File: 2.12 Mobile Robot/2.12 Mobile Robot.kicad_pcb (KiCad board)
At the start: 2 copper layers, 63 parts, among them J1 Motor Control L, J2 Motor Control R, J3 GND, J4 3.3V, J5 UART, J6 5V, J8 Power IO, Q1 DMMT5401-7-F, Q2 DMG2305UX-13, SW1 RST_SW, SW2 BOOT_SW, SW3 SW_PWR, SW4 SW_PWR, U1 ProS3, U2 TCA9548APWR, U3 MOTOR_PWR, U4 POWER_IN, U5 TPS564208DDCT

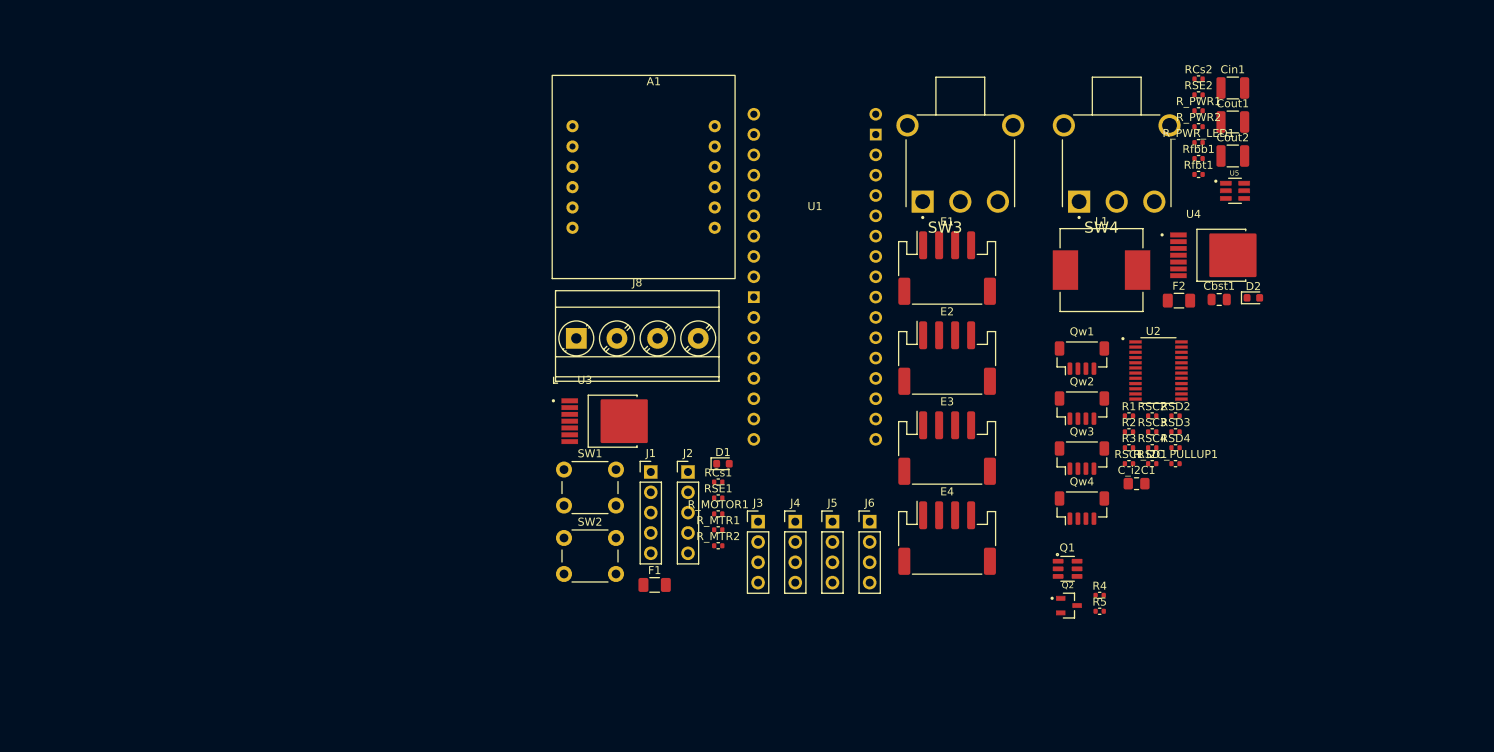
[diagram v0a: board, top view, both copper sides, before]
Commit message: Renamed stuff
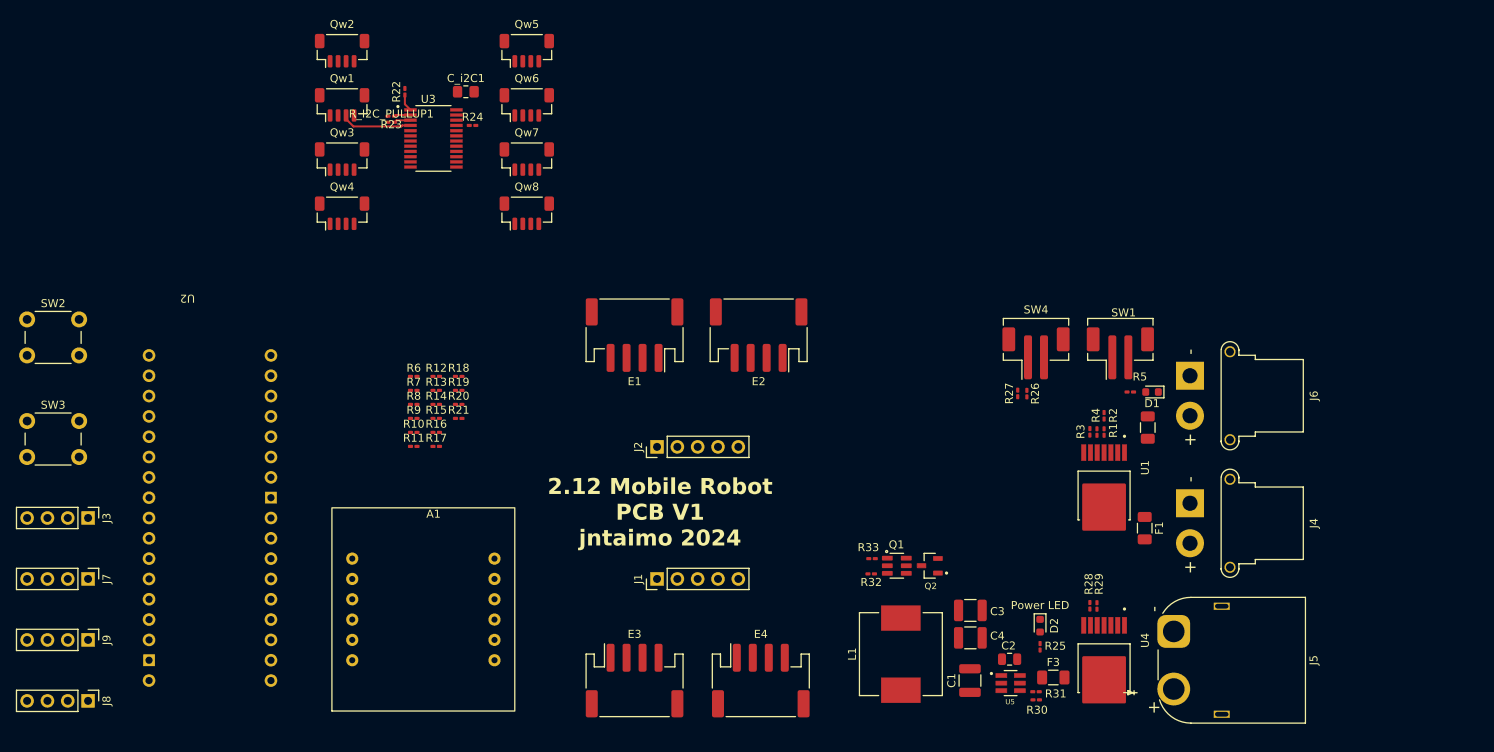
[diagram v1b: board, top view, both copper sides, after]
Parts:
- removed Cbst1: 0.1uF, Capacitor_SMD:C_0805_2012Metric
- removed Cin1: 10uF, Capacitor_SMD:C_1210_3225Metric
- removed Cout1, Cout2: 22uF, Capacitor_SMD:C_1210_3225Metric
- removed the F2 at (170.7, 89.7)
- removed the J8 at (95.3, 94.4)
- removed RCs2, RSE2, R_PWR1, R_PWR2: 15k, Resistor_SMD:R_0402_1005Metric
- removed RSC1, RSC2, RSC3, RSC4, RSD1, RSD2, RSD3, RSD4, Rfbb1: 10k, Resistor_SMD:R_0402_1005Metric
- removed R_PWR_LED1: 1kΩ, Resistor_SMD:R_0402_1005Metric
- removed Rfbt1: 56.2k, Resistor_SMD:R_0402_1005Metric
- added C1: 10uF, Capacitor_SMD:C_1210_3225Metric, F.Cu at (144.5, 137.2)
- added C2: 0.1uF, Capacitor_SMD:C_0805_2012Metric, F.Cu at (149.5, 134.5)
- added C3: 22uF, Capacitor_SMD:C_1210_3225Metric, F.Cu at (144.6, 128.4)
- added C4: 22uF, Capacitor_SMD:C_1210_3225Metric, F.Cu at (144.6, 131.8)
- added F1: 20A, Fuse:Fuse_1206_3216Metric, F.Cu at (166.4, 118.1)
- added F3: 20A, Fuse:Fuse_1206_3216Metric, F.Cu at (154.9, 136.8)
- added J4: Motor Power R, Connector_AMASS:AMASS_XT30PW-F_1x02_P2.50mm_Horizontal, F.Cu at (172.0, 115.0)
- added J5: Battery Power, Connector_AMASS:AMASS_XT60PW-M_1x02_P7.20mm_Horizontal, F.Cu at (170.0, 131.0)
- added J6: Motor Power L, Connector_AMASS:AMASS_XT30PW-F_1x02_P2.50mm_Horizontal, F.Cu at (172.0, 99.1)
- added Qw5: Qwiic, Connector_JST:JST_SH_BM04B-SRSS-TB_1x04-1MP_P1.00mm_Vertical, F.Cu at (89.1, 58.4)
- added Qw6: Qwiic, Connector_JST:JST_SH_BM04B-SRSS-TB_1x04-1MP_P1.00mm_Vertical, F.Cu at (89.1, 65.2)
- added Qw7: Qwiic, Connector_JST:JST_SH_BM04B-SRSS-TB_1x04-1MP_P1.00mm_Vertical, F.Cu at (89.1, 72.0)
- added Qw8: Qwiic, Connector_JST:JST_SH_BM04B-SRSS-TB_1x04-1MP_P1.00mm_Vertical, F.Cu at (89.1, 78.7)
- added R10: 10K, Resistor_SMD:R_0201_0603Metric_Pad0.64x0.40mm_HandSolder, F.Cu at (75.0, 106.1)
- added R11: 10K, Resistor_SMD:R_0201_0603Metric_Pad0.64x0.40mm_HandSolder, F.Cu at (75.0, 107.9)
- added R12: 10K, Resistor_SMD:R_0201_0603Metric_Pad0.64x0.40mm_HandSolder, F.Cu at (77.8, 99.1)
- added R13: 10K, Resistor_SMD:R_0201_0603Metric_Pad0.64x0.40mm_HandSolder, F.Cu at (77.8, 100.9)
- added R14: 10K, Resistor_SMD:R_0201_0603Metric_Pad0.64x0.40mm_HandSolder, F.Cu at (77.8, 102.6)
- added R15: 10K, Resistor_SMD:R_0201_0603Metric_Pad0.64x0.40mm_HandSolder, F.Cu at (77.8, 104.4)
- added R16: 10K, Resistor_SMD:R_0201_0603Metric_Pad0.64x0.40mm_HandSolder, F.Cu at (77.8, 106.1)
- added R17: 10K, Resistor_SMD:R_0201_0603Metric_Pad0.64x0.40mm_HandSolder, F.Cu at (77.8, 107.9)
- added R18: 10K, Resistor_SMD:R_0201_0603Metric_Pad0.64x0.40mm_HandSolder, F.Cu at (80.6, 99.1)
- added R19: 10K, Resistor_SMD:R_0201_0603Metric_Pad0.64x0.40mm_HandSolder, F.Cu at (80.6, 100.9)
- added R20: 10K, Resistor_SMD:R_0201_0603Metric_Pad0.64x0.40mm_HandSolder, F.Cu at (80.6, 102.6)
- added R21: 10K, Resistor_SMD:R_0201_0603Metric_Pad0.64x0.40mm_HandSolder, F.Cu at (80.6, 104.4)
- added R25: 1kΩ, Resistor_SMD:R_0201_0603Metric_Pad0.64x0.40mm_HandSolder, F.Cu at (153.3, 132.9)
- added R26: 15k, Resistor_SMD:R_0201_0603Metric_Pad0.64x0.40mm_HandSolder, F.Cu at (151.6, 101.3)
- added R27: 15k, Resistor_SMD:R_0201_0603Metric_Pad0.64x0.40mm_HandSolder, F.Cu at (150.5, 101.3)
- added R28: 15k, Resistor_SMD:R_0201_0603Metric_Pad0.64x0.40mm_HandSolder, F.Cu at (159.5, 127.8)
- added R29: 15k, Resistor_SMD:R_0201_0603Metric_Pad0.64x0.40mm_HandSolder, F.Cu at (160.4, 127.8)
- added R30: 56.2k, Resistor_SMD:R_0201_0603Metric_Pad0.64x0.40mm_HandSolder, F.Cu at (152.8, 139.6)
- added R31: 10k, Resistor_SMD:R_0201_0603Metric_Pad0.64x0.40mm_HandSolder, F.Cu at (152.8, 138.6)
- added R6: 10K, Resistor_SMD:R_0201_0603Metric_Pad0.64x0.40mm_HandSolder, F.Cu at (75.0, 99.1)
- added R7: 10K, Resistor_SMD:R_0201_0603Metric_Pad0.64x0.40mm_HandSolder, F.Cu at (75.0, 100.9)
- added R8: 10K, Resistor_SMD:R_0201_0603Metric_Pad0.64x0.40mm_HandSolder, F.Cu at (75.0, 102.6)
- added R9: 10K, Resistor_SMD:R_0201_0603Metric_Pad0.64x0.40mm_HandSolder, F.Cu at (75.0, 104.4)
- R1: renamed from R_MTR1; footprint Resistor_SMD:R_0402_1005Metric -> Resistor_SMD:R_0201_0603Metric_Pad0.64x0.40mm_HandSolder
- R2: renamed from R_MTR2; footprint Resistor_SMD:R_0402_1005Metric -> Resistor_SMD:R_0201_0603Metric_Pad0.64x0.40mm_HandSolder
- R22: renamed from R1; footprint Resistor_SMD:R_0402_1005Metric -> Resistor_SMD:R_0201_0603Metric_Pad0.64x0.40mm_HandSolder
- R23: renamed from R2; footprint Resistor_SMD:R_0402_1005Metric -> Resistor_SMD:R_0201_0603Metric_Pad0.64x0.40mm_HandSolder
- R24: renamed from R3; footprint Resistor_SMD:R_0402_1005Metric -> Resistor_SMD:R_0201_0603Metric_Pad0.64x0.40mm_HandSolder
- R3: renamed from RSE1; footprint Resistor_SMD:R_0402_1005Metric -> Resistor_SMD:R_0201_0603Metric_Pad0.64x0.40mm_HandSolder
- R32: renamed from R4; footprint Resistor_SMD:R_0402_1005Metric -> Resistor_SMD:R_0201_0603Metric_Pad0.64x0.40mm_HandSolder
- R33: renamed from R5; footprint Resistor_SMD:R_0402_1005Metric -> Resistor_SMD:R_0201_0603Metric_Pad0.64x0.40mm_HandSolder
- R4: renamed from RCs1; footprint Resistor_SMD:R_0402_1005Metric -> Resistor_SMD:R_0201_0603Metric_Pad0.64x0.40mm_HandSolder
- R5: renamed from R_MOTOR1; footprint Resistor_SMD:R_0402_1005Metric -> Resistor_SMD:R_0201_0603Metric_Pad0.64x0.40mm_HandSolder
- R_I2C_PULLUP1: footprint Resistor_SMD:R_0402_1005Metric -> Resistor_SMD:R_0201_0603Metric_Pad0.64x0.40mm_HandSolder
- SW1: renamed from SW3; footprint 2.679:SW_500SSP1S1M6QEA -> Connector_JST:JST_PH_B2B-PH-SM4-TB_1x02-1MP_P2.00mm_Vertical
- SW4: footprint 2.679:SW_500SSP1S1M6QEA -> Connector_JST:JST_PH_B2B-PH-SM4-TB_1x02-1MP_P2.00mm_Vertical
- moved R_I2C_PULLUP1 106.9 mm to (72.2, 67.4)
- moved Qw2 102.7 mm to (66.0, 58.4)
- moved R23 100.3 mm to (72.2, 66.6), turned to 180 degrees
- moved Qw3 99.7 mm to (66.0, 72.0)
- moved Qw4 99.6 mm to (66.0, 78.7)
- moved R22 99.2 mm to (73.9, 63.6), turned to 90 degrees
- moved J9 98.8 mm to (34.3, 132.1), turned to -90 degrees
- moved Qw1 97.7 mm to (66.0, 65.2)
- moved C_i2C1 97.1 mm to (81.5, 63.6)
- moved J8 95.7 mm to (34.3, 139.7), turned to -90 degrees
- moved U3 95.2 mm to (77.5, 69.4)
- moved R24 91.4 mm to (82.3, 67.8)
- moved J7 88.7 mm to (34.3, 124.5), turned to -90 degrees
- moved J3 83.8 mm to (34.3, 116.8), turned to -90 degrees
- moved U2 81.4 mm to (49.5, 116.8), turned to 180 degrees
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- renumbered F1 to F2, J2 to J1, J1 to J2, J4 to J7, J5 to J8, J6 to J9, SW1 to SW2, SW2 to SW3, U3 to U1, U1 to U2, U2 to U3
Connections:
- net /VBAT_MCU renamed /Buck/VBAT_MCU
- F2 pad 2: /VBAT_MOTOR_PRE -> Net-(F2-Pad2)
- J9 pad 1: /BUCK_5V -> +5V
- J9 pad 2: /BUCK_5V -> +5V
- J9 pad 3: /BUCK_5V -> +5V
- J9 pad 4: /BUCK_5V -> +5V
- U1 pad 1: /VBAT_MOTOR_PRE -> /VBAT_MOTOR
- U1 pad 2: /VBAT_MOTOR_PRE -> /VBAT_MOTOR
- U1 pad 3: /VBAT_MOTOR_PRE -> /VBAT_MOTOR
- U3 pad 13: unconnected-(U2-SD4-Pad13) -> /Qwiic/SD4
- U3 pad 14: unconnected-(U2-SC4-Pad14) -> /Qwiic/SC4
- U3 pad 15: unconnected-(U2-SD5-Pad15) -> /Qwiic/SD5
- U3 pad 16: unconnected-(U2-SC5-Pad16) -> /Qwiic/SC5
- U3 pad 17: unconnected-(U2-SD6-Pad17) -> /Qwiic/SD6
- U3 pad 18: unconnected-(U2-SC6-Pad18) -> /Qwiic/SC6
- U3 pad 19: unconnected-(U2-SD7-Pad19) -> /Qwiic/SD7
- U3 pad 20: unconnected-(U2-SC7-Pad20) -> /Qwiic/SC7
- U4 pad 1: /VBAT -> /Buck/VBAT
- U4 pad 2: /VBAT -> /Buck/VBAT
- U4 pad 3: /VBAT -> /Buck/VBAT
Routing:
- net /Qwiic/SD0: track 0.00 -> 8.93 mm
- net Net-(U3-A0): track 0.00 -> 2.14 mm
- net Net-(U3-~{RESET}): track 0.00 -> 2.10 mm
- net Net-(U3-A1): track 0.00 -> 2.05 mm
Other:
- board text added: "2.12 Mobile Robot PCB V1 jntaimo 2024"

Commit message: Fully routed
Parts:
- added ?: , , F.Cu at (200.0, 136.0)
- added ?: , , F.Cu at (40.0, 136.0)
- added ?: , , F.Cu at (200.0, 96.0)
- added REF**: MountingHole_4.3mm_M4_DIN965_Pad, MountingHole:MountingHole_4.3mm_M4_DIN965_Pad, F.Cu at (40.0, 96.0)
- J1: value Motor Control R -> Motor R
- J2: value Motor Control L -> Motor L
- SW2: value RST_SW -> RST
- SW3: value BOOT_SW -> BOOT
- moved J3 69.4 mm to (103.5, 121.5)
- moved J8 69.3 mm to (103.5, 136.8)
- moved J7 69.3 mm to (103.5, 126.6)
- moved J9 69.2 mm to (103.5, 131.7)
- moved SW2 55.7 mm to (63.6, 133.8)
- moved R22 52.9 mm to (55.3, 113.1), turned to -90 degrees
- moved Qw2 50.4 mm to (49.0, 105.8), turned to 90 degrees
- moved Qw8 49.6 mm to (69.4, 124.2), turned to -90 degrees
- moved R23 49.1 mm to (56.2, 113.1), turned to -90 degrees
- moved Qw4 48.5 mm to (49.0, 124.2), turned to 90 degrees
- moved R25 48.1 mm to (57.0, 113.1), turned to 90 degrees
- moved E3 47.7 mm to (128.5, 97.1), turned to 180 degrees
- moved Qw7 47.4 mm to (69.4, 115.0), turned to -90 degrees
- moved C1 46.9 mm to (54.5, 102.0), turned to 90 degrees
- moved E4 46.7 mm to (142.5, 97.1), turned to 180 degrees
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- renumbered C_i2C1 to C1, C1 to C2, C2 to C3, C3 to C4, C4 to C5, R_I2C_PULLUP1 to R25, R25 to R26, R26 to R27, R27 to R28, R28 to R29, R29 to R30, R30 to R31, R31 to R32, R32 to R33, R33 to R34
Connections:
- net Net-(F1-Pad2) renamed /R_MOTOR
- net Net-(F2-Pad2) renamed /L_MOTOR
- F3 pad 1: /Buck/VBAT -> /VBAT
- U4 pad 1: /Buck/VBAT -> /VBAT
- U4 pad 2: /Buck/VBAT -> /VBAT
- U4 pad 3: /Buck/VBAT -> /VBAT
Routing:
- net /IMU_RST: track 0.00 -> 113.2 mm
- net /SDA: track 0.00 -> 103.7 mm, vias 0 -> 3
- net /IMU_CS: track 0.00 -> 82.6 mm
- net /SCL: track 0.00 -> 80.5 mm, vias 0 -> 1
- net /IMU_INT: track 0.00 -> 80.1 mm
- net /HALL_BR_A: track 0.00 -> 79.8 mm
- net +5V: track 0.00 -> 75.6 mm
- net /HALL_BR_B: track 0.00 -> 74.3 mm
- net GND: track 0.00 -> 72.9 mm, vias 0 -> 189
- net /PWM1_R: track 0.00 -> 71.6 mm
- net /HALL_FR_A: track 0.00 -> 69.8 mm, vias 0 -> 2
- net /DIR2_R: track 0.00 -> 69.1 mm
- net /HALL_BL_A: track 0.00 -> 57.3 mm
- net +3.3V: track 0.00 -> 54.5 mm, vias 0 -> 21
- net /HALL_FR_B: track 0.00 -> 51.8 mm, vias 0 -> 4
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- added copper zone on In2.Cu, net +3.3V
- added copper zone on F.Cu, net /BUCK_5V
- added copper zone on In1.Cu, net /BUCK_5V
- added copper zone on In2.Cu, net /BUCK_5V
- added copper zone on B.Cu, net /R_MOTOR
- added copper zone on F.Cu, net /R_MOTOR
- added copper zone on In1.Cu, net /R_MOTOR
- added copper zone on In2.Cu, net /R_MOTOR
- added copper zone on B.Cu, net /VBAT
- added copper zone on F.Cu, net /VBAT
- added copper zone on In1.Cu, net /VBAT
- added copper zone on In2.Cu, net /VBAT
- added copper zone on B.Cu, net /VBAT_IN
- added copper zone on F.Cu, net /VBAT_IN
- added copper zone on In1.Cu, net /VBAT_IN
- added copper zone on In2.Cu, net /VBAT_IN
- added copper zone on B.Cu, net /VBAT_MOTOR
- added copper zone on F.Cu, net /VBAT_MOTOR
- added copper zone on In1.Cu, net /VBAT_MOTOR
- added copper zone on In2.Cu, net /VBAT_MOTOR
- added copper zone on B.Cu, net GND
- added copper zone on F.Cu, net GND
- added copper zone on In1.Cu, net GND
- added copper zone on In2.Cu, net GND
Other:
- board outline added: 176 x 56 mm
- copper layers 2 -> 4
- board text added: "3V"
- board text added: "BLA"
- board text added: "BLB"
- board text added: "BRA"
- board text added: "BRB"
- board text added: "BUCK"
- board text added: "D1"
- board text added: "D2"
- board text added: "FLA"
- board text added: "FLB"
- board text added: "FRA"
- board text added: "FRB"
- board text added: "G"
- board text added: "I2C"
- board text added: "IMU"
- board text added: "MOTOR"
- board text added: "P1"
- board text added: "P2"
- board text added: "RX"
- board text added: "TX"
- board text added: "USB"
- board text added: "ZVD"

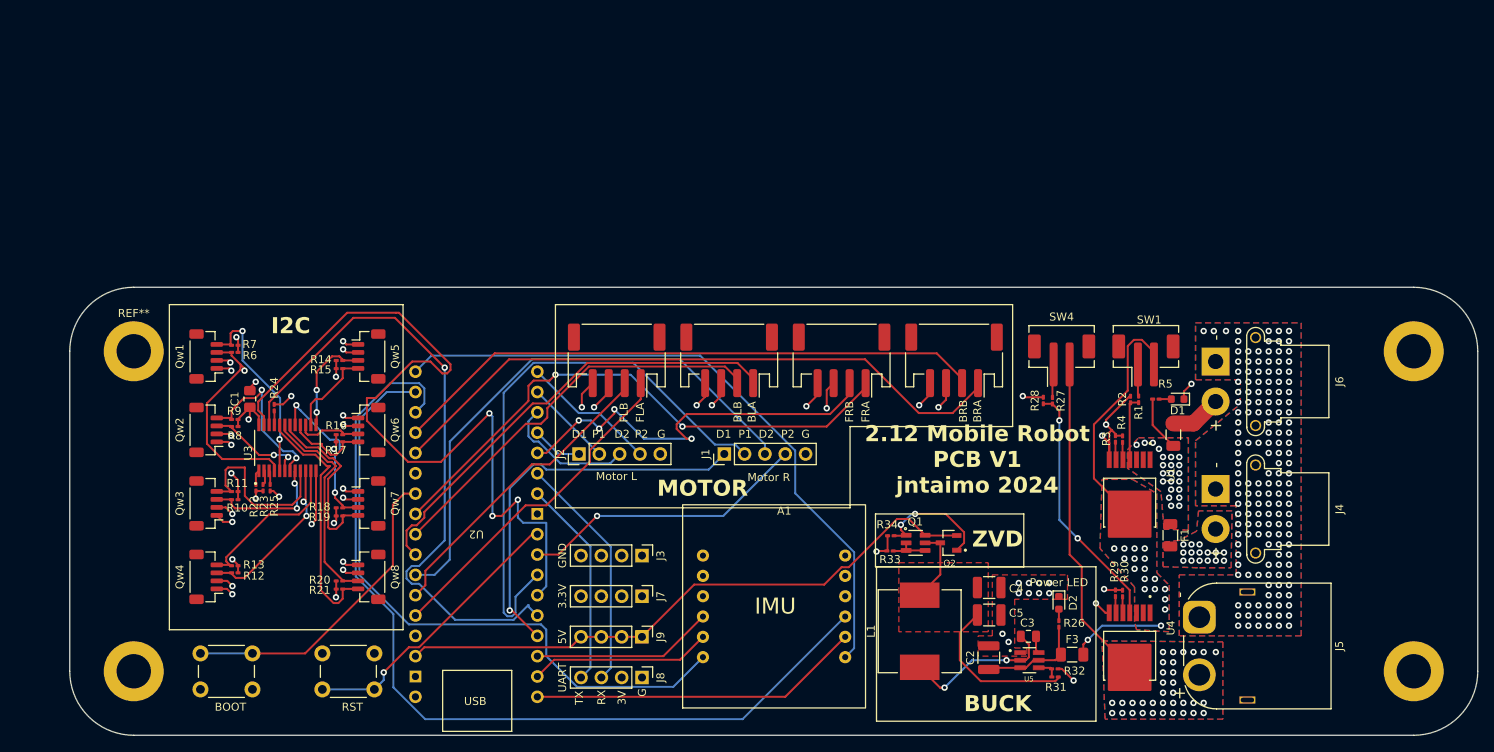
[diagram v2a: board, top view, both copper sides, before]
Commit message: Made footprints from project libraries
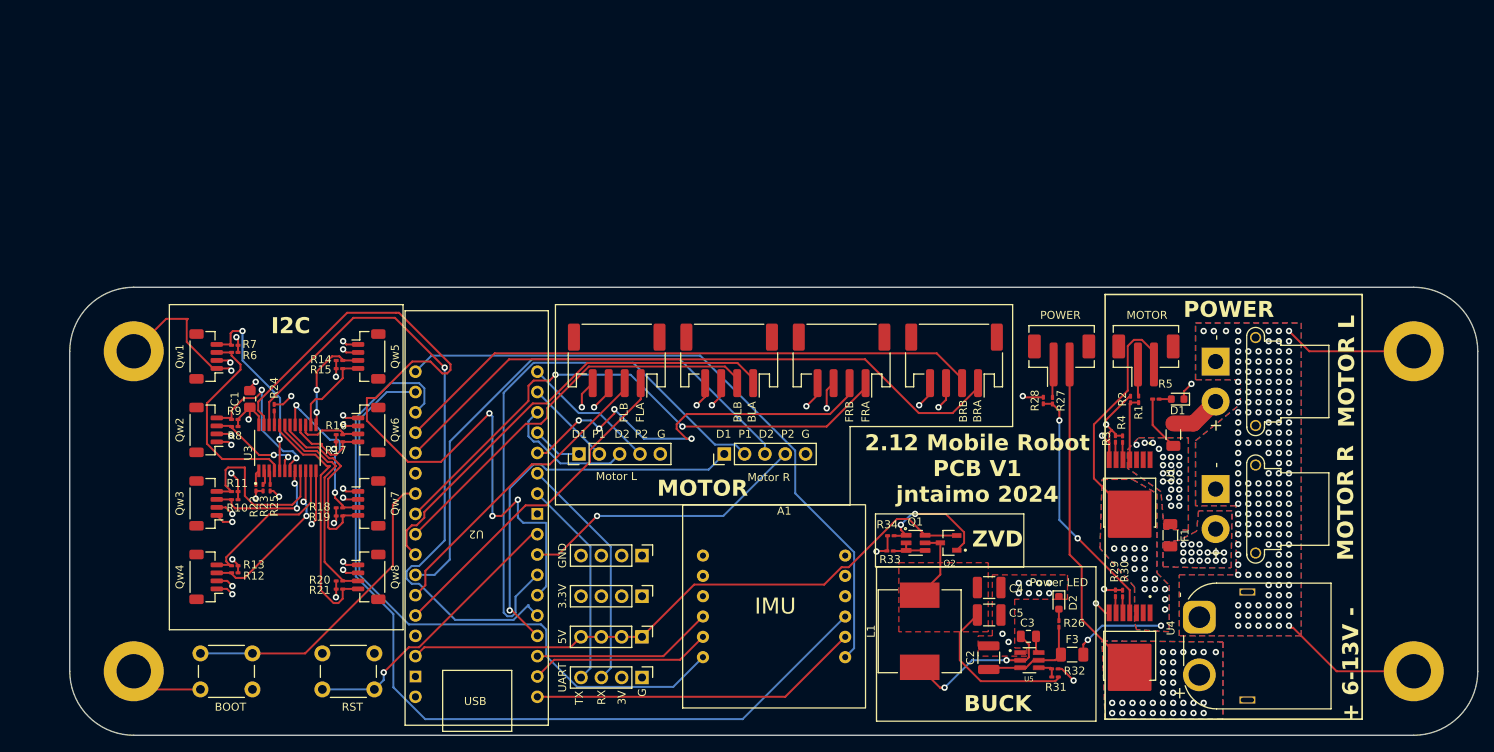
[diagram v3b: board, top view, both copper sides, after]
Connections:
- REF** pad 1: (no net) -> GND
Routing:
- net GND: track 72.9 -> 133.3 mm
- net /Qwiic/SD0: track 26.8 -> 25.8 mm, vias 1 -> 0
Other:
- board text added: "+ 6-13V -"
- board text added: "MOTOR L"
- board text added: "MOTOR R"
- board text added: "POWER"
